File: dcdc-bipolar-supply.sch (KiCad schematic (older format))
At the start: 14 parts

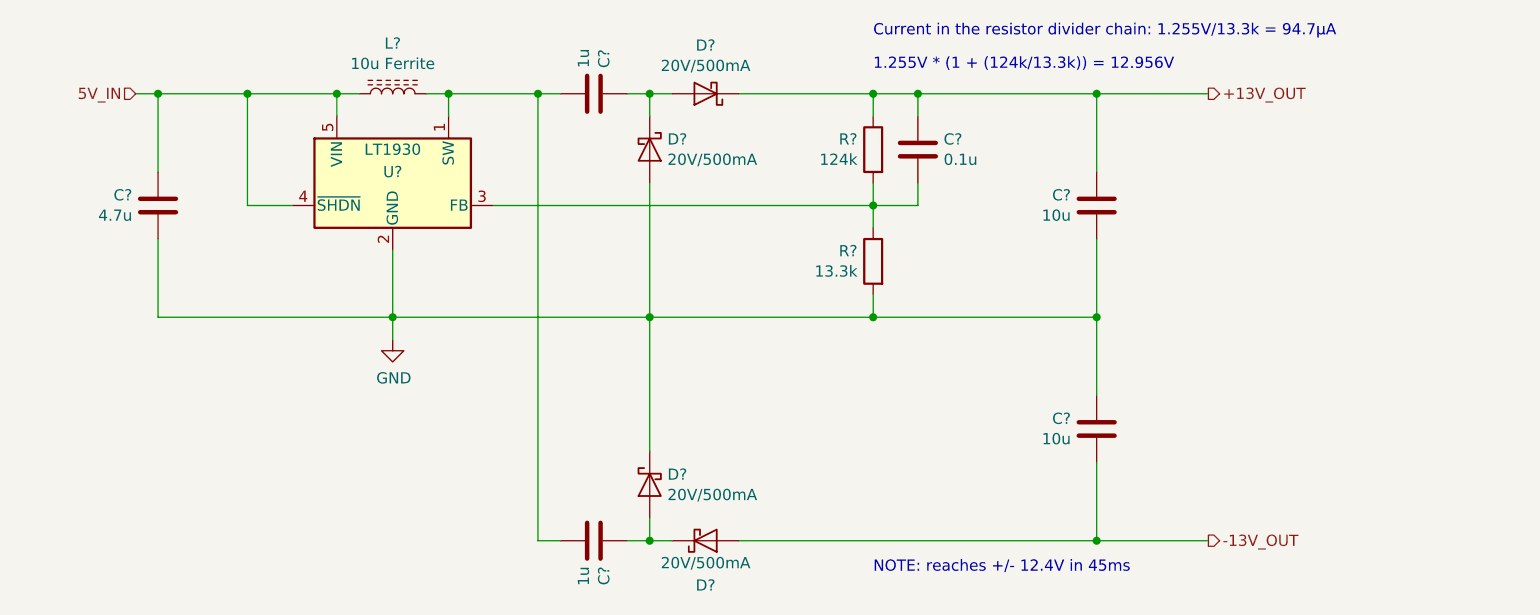
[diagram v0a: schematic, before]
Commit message: update dcdc feedback config & components
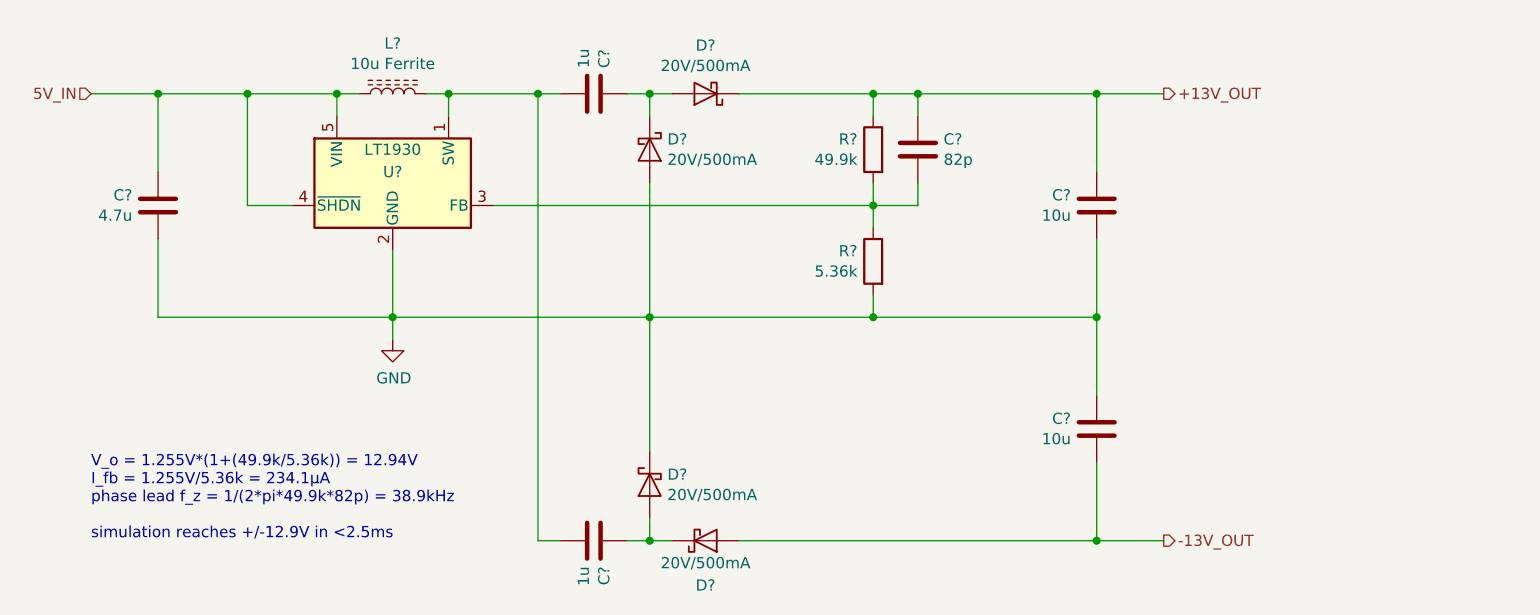
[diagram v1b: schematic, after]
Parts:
- C?: value 0.1u -> 82p; Description CAP CER 0.1UF 50V X7R 0805 -> CAP CER 82PF 50V NPO 0805; Manufacturer Samsung Electro-Mechanics -> Yageo; Manufacturer Part Number CL21B104JBCNNNC -> CC0805FRNPO9BN820; Supplier Part Number 1276-1090-1-ND -> 311-4183-1-ND
- R?: value 124k -> 49.9k; Description RES SMD 124K OHM 1% 1/8W 0805 -> RES SMD 49.9K OHM 1% 1/8W 0805; Manufacturer Part Number ERJ-6ENF1243V -> ERJ-6ENF4992V; Supplier Part Number P124KCCT-ND -> P49.9KCCT-ND
- R?: value 13.3k -> 5.36k; Description RES SMD 13.3K OHM 1% 1/8W 0805 -> RES SMD 5.36K OHM 1% 1/8W 0805; Manufacturer Part Number ERJ-6ENF1332V -> ERJ-6ENF5361V; Supplier Part Number P13.3KCCT-ND -> P5.36KCCT-ND
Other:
- note added: "V_o = 1.255V*(1+(49.9k/5.36k)) = 12.94V\nI_fb = 1.255V/5.36k = 234.1µA\nphase lead f_z = 1/(2*pi*49.9k*82p) = 38.9kHz\n\nsimulation reaches +/-12.9V in <2.5ms"
- note removed: "1.255V * (1 + (124k/13.3k)) = 12.956V"
- note removed: "Current in the resistor divider chain: 1.255V/13.3k = 94.7µA"
- note removed: "NOTE: reaches +/- 12.4V in 45ms"
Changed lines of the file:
@@
 Comment4 ""
 $EndDescr
-Text HLabel 3200 3050 0    50   Input ~ 0
+Text HLabel 3000 3050 0    50   Input ~ 0
 5V_IN
 $Comp
@@
 P 6500 3300
 F 0 "R?" H 6570 3346 50  0000 L CNN
-F 1 "124k" H 6570 3255 50  0000 L CNN
+F 1 "49.9k" H 6570 3255 50  0000 L CNN
 F 2 "Resistor_SMD:R_0805_2012Metric_Pad1.15x1.40mm_HandSolder" V 6430 3300 50  0001 C CNN
 F 3 "https://industrial.panasonic.com/cdbs/www-data/pdf/RDA0000/AOA0000C304.pdf" H 6500 3300 50  0001 C CNN
-F 4 "RES SMD 124K OHM 1% 1/8W 0805" H 0   0   50  0001 C CNN "Description"
+F 4 "RES SMD 49.9K OHM 1% 1/8W 0805" H 0   0   50  0001 C CNN "Description"
 F 5 "Panasonic Electronic Components" H 0   0   50  0001 C CNN "Manufacturer"
-F 6 "ERJ-6ENF1243V" H 0   0   50  0001 C CNN "Manufacturer Part Number"
-F 7 "Digi-Key" H 0   0   50  0001 C CNN "Supplier"
-F 8 "P124KCCT-ND" H 0   0   50  0001 C CNN "Supplier Part Number"
+F 6 "ERJ-6ENF4992V" H 0   0   50  0001 C CNN "Manufacturer Part Number"
+F 7 "Digi-Key" H 0   0   50  0001 C CNN "Supplier"
+F 8 "P49.9KCCT-ND" H 0   0   50  0001 C CNN "Supplier Part Number"
 	1    6500 3300
 	-1   0    0    -1
@@
 P 6500 3800
 F 0 "R?" H 6570 3846 50  0000 L CNN
-F 1 "13.3k" H 6570 3755 50  0000 L CNN
+F 1 "5.36k" H 6570 3755 50  0000 L CNN
 F 2 "Resistor_SMD:R_0805_2012Metric_Pad1.15x1.40mm_HandSolder" V 6430 3800 50  0001 C CNN
 F 3 "https://industrial.panasonic.com/cdbs/www-data/pdf/RDA0000/AOA0000C304.pdf" H 6500 3800 50  0001 C CNN
-F 4 "RES SMD 13.3K OHM 1% 1/8W 0805" H 0   0   50  0001 C CNN "Description"
+F 4 "RES SMD 5.36K OHM 1% 1/8W 0805" H 0   0   50  0001 C CNN "Description"
 F 5 "Panasonic Electronic Components" H 0   0   50  0001 C CNN "Manufacturer"
-F 6 "ERJ-6ENF1332V" H 0   0   50  0001 C CNN "Manufacturer Part Number"
-F 7 "Digi-Key" H 0   0   50  0001 C CNN "Supplier"
-F 8 "P13.3KCCT-ND" H 0   0   50  0001 C CNN "Supplier Part Number"
+F 6 "ERJ-6ENF5361V" H 0   0   50  0001 C CNN "Manufacturer Part Number"
+F 7 "Digi-Key" H 0   0   50  0001 C CNN "Supplier"
+F 8 "P5.36KCCT-ND" H 0   0   50  0001 C CNN "Supplier Part Number"
 	1    6500 3800
 	-1   0    0    -1
@@
 	6500 3550 6500 3650
 Connection ~ 6500 3550
-Text HLabel 8000 3050 2    50   Output ~ 0
+Text HLabel 7800 3050 2    50   Output ~ 0
 +13V_OUT
 Wire Wire Line
@@
 Connection ~ 7500 3050
 Wire Wire Line
-	7500 3050 8000 3050
+	7500 3050 7800 3050
 Wire Wire Line
 	7500 3700 7500 4050
@@
 	5900 3050 6500 3050
 Connection ~ 6500 3050
-Text HLabel 8000 5050 2    50   Output ~ 0
+Text HLabel 7800 5050 2    50   Output ~ 0
 -13V_OUT
 Wire Wire Line
-	7500 5050 8000 5050
+	7500 5050 7800 5050
 Connection ~ 7500 5050
 Wire Wire Line
@@
 Connection ~ 4100 3050
 Wire Wire Line
-	3200 3050 3300 3050
+	3000 3050 3300 3050
 Wire Wire Line
 	3300 3050 3300 3400
@@
 AR Path="/5C903B7C/5CA5C6DD" Ref="C?"  Part="1"
 F 0 "C?" H 6585 3254 50  0000 R CNN
-F 1 "0.1u" H 6585 3345 50  0000 R CNN
+F 1 "82p" H 6585 3345 50  0000 R CNN
 F 2 "Capacitor_SMD:C_0805_2012Metric_Pad1.15x1.40mm_HandSolder" H 6738 3150 50  0001 C CNN
-F 3 "http://www.samsungsem.com/kr/support/product-search/mlcc/__icsFiles/afieldfile/2018/07/23/CL21B104JBCNNNC.pdf" H 6700 3300 50  0001 C CNN
-F 4 "CAP CER 0.1UF 50V X7R 0805" H 0   0   50  0001 C CNN "Description"
-F 5 "Samsung Electro-Mechanics" H 0   0   50  0001 C CNN "Manufacturer"
-F 6 "CL21B104JBCNNNC" H 0   0   50  0001 C CNN "Manufacturer Part Number"
-F 7 "Digi-Key" H 0   0   50  0001 C CNN "Supplier"
-F 8 "1276-1090-1-ND" H 0   0   50  0001 C CNN "Supplier Part Number"
+F 3 "http://www.yageo.com/documents/recent/UPY-GP_NP0_16V-to-50V_16.pdf" H 6700 3300 50  0001 C CNN
+F 4 "CAP CER 82PF 50V NPO 0805" H 0   0   50  0001 C CNN "Description"
+F 5 "Yageo" H 0   0   50  0001 C CNN "Manufacturer"
+F 6 "CC0805FRNPO9BN820" H 0   0   50  0001 C CNN "Manufacturer Part Number"
+F 7 "Digi-Key" H 0   0   50  0001 C CNN "Supplier"
+F 8 "311-4183-1-ND" H 0   0   50  0001 C CNN "Supplier Part Number"
 	1    6700 3300
 	-1   0    0    1
@@
 Wire Wire Line
 	6700 3050 7500 3050
-Text Notes 6500 2950 0    50   ~ 0
-1.255V * (1 + (124k/13.3k)) = 12.956V
-Text Notes 6500 5200 0    50   ~ 0
-NOTE: reaches +/- 12.4V in 45ms
-Text Notes 6500 2800 0    50   ~ 0
-Current in the resistor divider chain: 1.255V/13.3k = 94.7µA
+Text Notes 3000 5050 0    50   ~ 0
+V_o = 1.255V*(1+(49.9k/5.36k)) = 12.94V\nI_fb = 1.255V/5.36k = 234.1µA\nphase lead f_z = 1/(2*pi*49.9k*82p) = 38.9kHz\n\nsimulation reaches +/-12.9V in <2.5ms
 $EndSCHEMATC

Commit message: switch components supplier to Mouser for price/availability
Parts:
- C?: Supplier Digi-Key -> Mouser; Supplier Part Number 587-1297-1-ND -> 963-LMK212BJ475KD-T
- U?: Supplier Digi-Key -> Mouser; Supplier Part Number LT1930ES5#TRPBFCT-ND -> 584-LT1930ES5#TRPBF
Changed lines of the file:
@@
 F 5 "Taiyo Yuden" H 0   0   50  0001 C CNN "Manufacturer"
 F 6 "LMK212BJ475KD-T" H 0   0   50  0001 C CNN "Manufacturer Part Number"
-F 7 "Digi-Key" H 0   0   50  0001 C CNN "Supplier"
-F 8 "587-1297-1-ND" H 0   0   50  0001 C CNN "Supplier Part Number"
+F 7 "Mouser" H 0   0   50  0001 C CNN "Supplier"
+F 8 "963-LMK212BJ475KD-T" H 0   0   50  0001 C CNN "Supplier Part Number"
 	1    3300 3550
 	1    0    0    1
@@
 F 5 "Linear Technology" H 0   0   50  0001 C CNN "Manufacturer"
 F 6 "LT1930ES5#TRPBF" H 0   0   50  0001 C CNN "Manufacturer Part Number"
-F 7 "Digi-Key" H 0   0   50  0001 C CNN "Supplier"
-F 8 "LT1930ES5#TRPBFCT-ND" H 0   0   50  0001 C CNN "Supplier Part Number"
+F 7 "Mouser" H 0   0   50  0001 C CNN "Supplier"
+F 8 "584-LT1930ES5#TRPBF" H 0   0   50  0001 C CNN "Supplier Part Number"
 	1    4350 3450
 	1    0    0    -1

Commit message: add circuit notes
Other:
- note added: "V_o = 1.255V*(1+(49.9k/5.36k)) = 12.94V\nI_fb = 1.255V/5.36k = 234.1µA\n\nphase lead f_z = 1/(2*pi*49.9k*82p) = 38.9kHz\n—> within the recommended range (35kHz-55kHz)\n\nsimulation reaches +/-12.9V in <2.5ms"
- note removed: "V_o = 1.255V*(1+(49.9k/5.36k)) = 12.94V\nI_fb = 1.255V/5.36k = 234.1µA\nphase lead f_z = 1/(2*pi*49.9k*82p) = 38.9kHz\n\nsimulation reaches +/-12.9V in <2.5ms"
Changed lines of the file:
@@
 	6700 3050 7500 3050
 Text Notes 3000 5050 0    50   ~ 0
-V_o = 1.255V*(1+(49.9k/5.36k)) = 12.94V\nI_fb = 1.255V/5.36k = 234.1µA\nphase lead f_z = 1/(2*pi*49.9k*82p) = 38.9kHz\n\nsimulation reaches +/-12.9V in <2.5ms
+V_o = 1.255V*(1+(49.9k/5.36k)) = 12.94V\nI_fb = 1.255V/5.36k = 234.1µA\n\nphase lead f_z = 1/(2*pi*49.9k*82p) = 38.9kHz\n—> within the recommended range (35kHz-55kHz)\n\nsimulation reaches +/-12.9V in <2.5ms
 $EndSCHEMATC
